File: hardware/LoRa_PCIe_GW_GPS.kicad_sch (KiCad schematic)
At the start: 11 parts, among them Q600 NC, U600 ZOE-M8Q

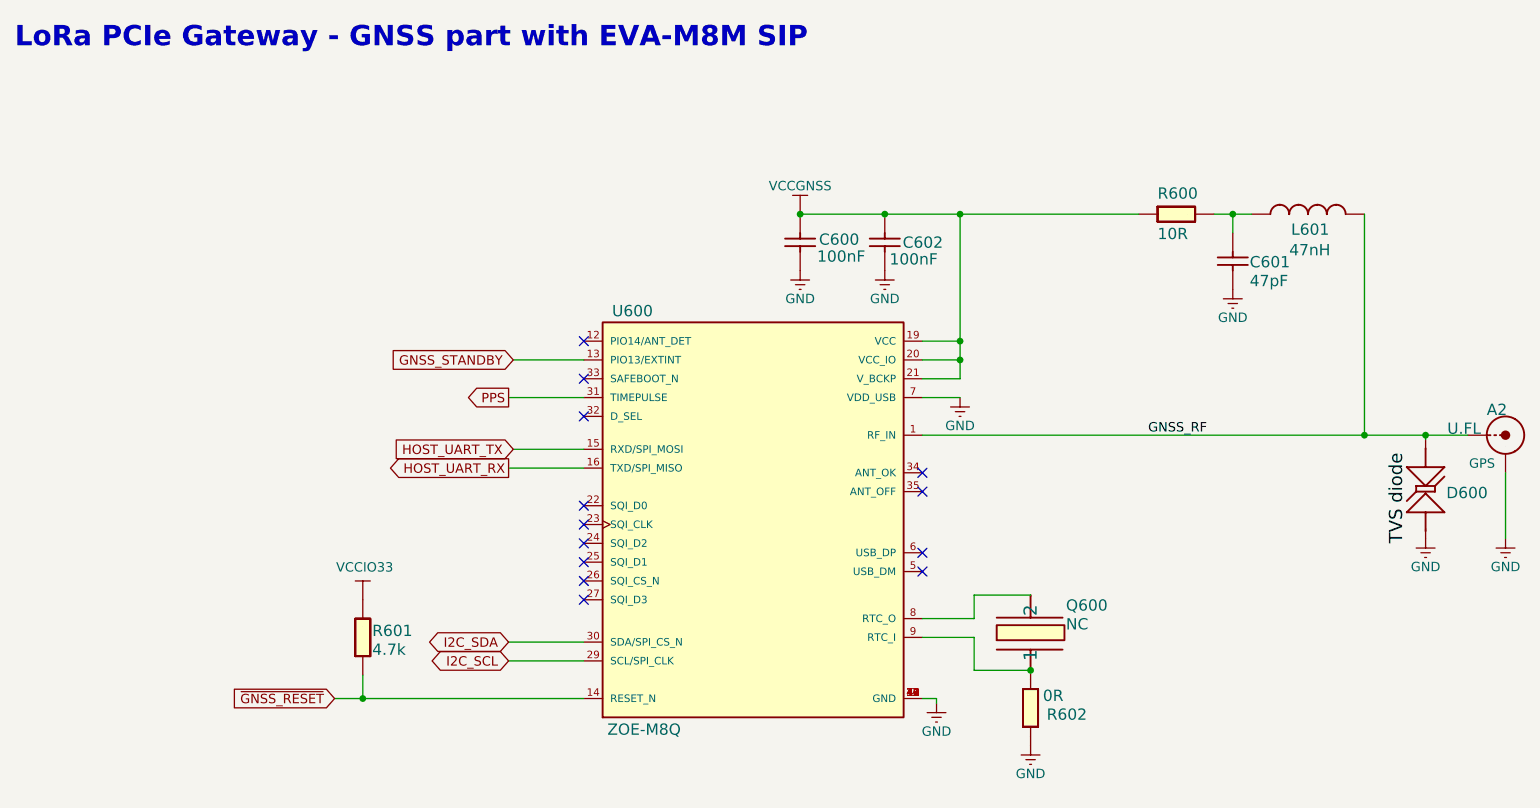
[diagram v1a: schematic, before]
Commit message: Fixed ERC and Schematic to Layout parity errors.
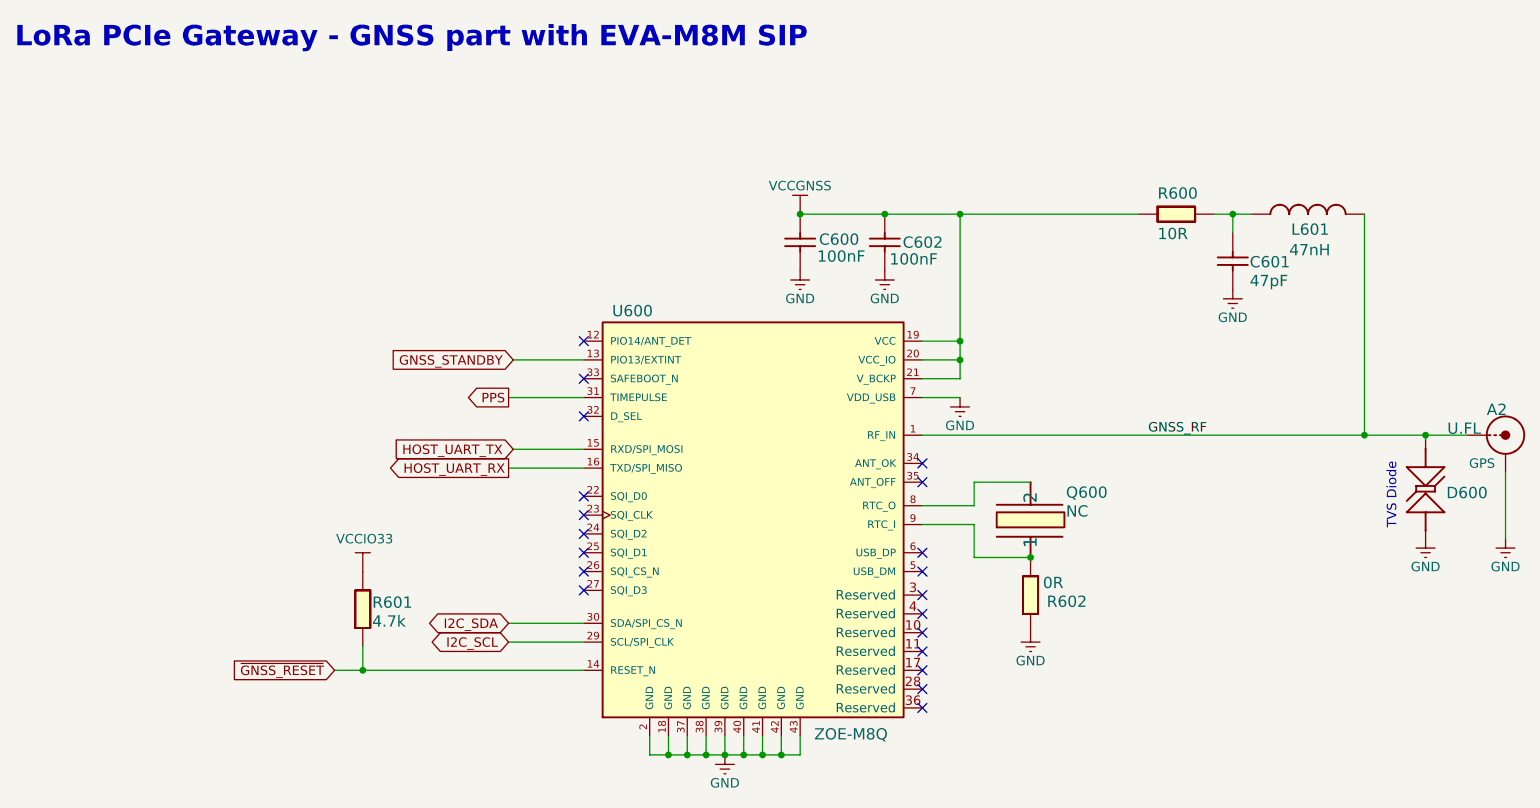
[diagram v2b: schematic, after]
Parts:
- U600: footprint LoRa_PCIe_GW:LGA43R65P9X9_700X700X116 -> LGA43R65P9X9_700X700X116; MANUFACTURER (none) -> UBLOX; PART_REV (none) -> R02; STANDARD (none) -> IPC7351B
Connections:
- no-connect marks 13 -> 20
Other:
- note added: "TVS Diode"
- moved on the sheet: Q600, R601, R602
